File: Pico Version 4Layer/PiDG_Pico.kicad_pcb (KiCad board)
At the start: 4 copper layers, 126 x 126 mm, 70 parts, among them J1 Conn_02x05_Odd_Even, J10 Trig, J11 Laser Enable, J12 Pixel Reset, J14 Pico Socket A, J15 Pico Socket B, J16 Laser En/PWM Trig/GND, J17 USB-C PD in, J2 Conn_02x05_Odd_Even, J3 Conn_02x05_Odd_Even, J4 Conn_02x05_Odd_Even, J5 Conn_02x05_Odd_Even, J6 Conn_02x05_Odd_Even, J7 Laser 1, J8 Laser 2, U1 74LVC1G04, U10 74AHCT1G08, U12 74LVC1G17, U13 UCC27524, U14 CH224K, U15 AP63205WU, U16 LM66100, U17 LP2951D, U2 SN74LVC04AD, U3 74LVC1G04, U4 SN74LVC04AD, U5 74LVC1G04, U6 SN74LVC04AD, U7 74AHCT1G08, U8 74AHCT1G08, U9 NCP718xSN180

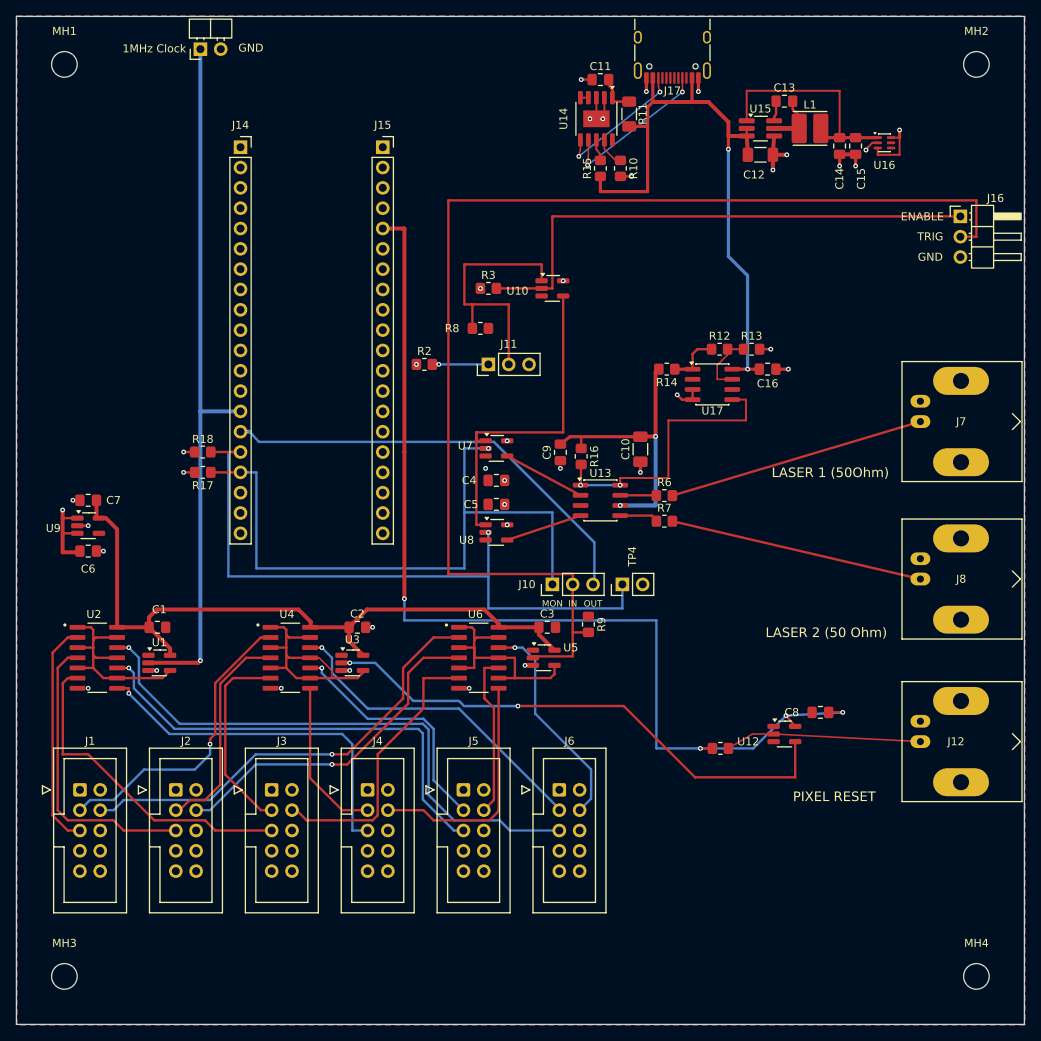
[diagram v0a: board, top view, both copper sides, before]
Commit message: Final DFM/SI review: layout fixes, fresh fab outputs, JLC files, README
Board (Pico Version 4Layer), from a fab / assembly / signal-integrity review:
- U13 decoupling: C9 (0.1 uF 50 V) moved beside VDD pin 6 with its own GND
  via; GND pin 3 gets a direct plane via; +12V via moved under the package;
  R6/R7 shifted 2 mm out to make room. Loop ~1.5-2 nH, was 7-13 nH.
- R19 100 ohm in series with J10 pin 1 (new net CH1_J10): with J10 on 1-2,
  the PWM_TRIG_TAP load made CH1 arrive 0.4-1.7 ns after CH2.
- No vias left inside SMD pads except U14's exposed-pad thermal vias:
  13 moved off their pads (U13 ENA/ENB now joined on F.Cu), 9 nudged clear
  of neighbouring mask openings.
- 47 edge stitching vias and 7 local GND vias at decoupling caps / IC grounds.
- 3 mm copper keep-out around each M3 hole; zone-to-edge clearance 0.5 mm.
- Silkscreen: TP3 reference restored ("1MHz Clock" kept as board text),
  J10 relabelled CH1/TRG/MKR, J11 ON/OFF, Pico outline + USB-end arrow +
  pin-1 mark, references moved off vias.
- U11 (socketed Pico) marked not-on-board / not-in-BOM in the schematic.
DRC 0 violations / 0 unconnected, ERC 0, all 334 pads match the schematic.

Outputs: gerbers, drills and zip regenerated (the previous set predated the
silkscreen edits); BOM/CPL updated (R19, capacitor voltage/dielectric,
loose jumper shunts); fab/jlc/ holds JLC-format SMD BOM and CPL with the
LCSC column left for part selection.

Docs: new top-level README (quick start, connecting, full command reference
with replies captured from the firmware, troubleshooting, wireless as a
future option); tools/pidg_example.py; Hardware.md gains manufacturing notes
and first-power-up checks and loses stale claims (finest pitch, RUN button,
TX_DROPPED unit, J16 interlock, Wi-Fi range).

Co-Authored-By: Claude Opus 5.5 (1M context) <noreply@anthropic.com>
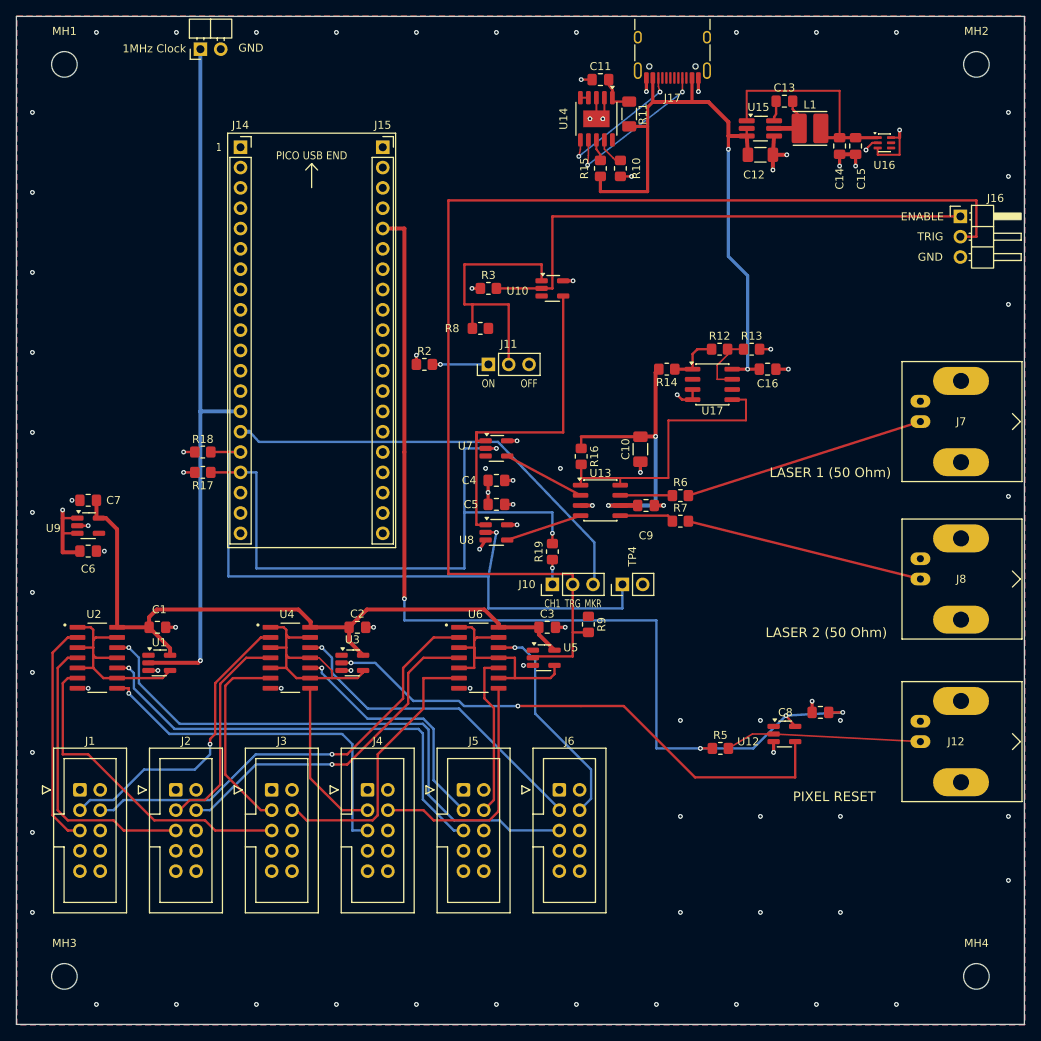
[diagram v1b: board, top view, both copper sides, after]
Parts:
- added R19: 100, Resistor_SMD:R_0805_2012Metric_Pad1.20x1.40mm_HandSolder, F.Cu at (199.0, 96.9)
- TP3: renamed from 1MHz Clock
- moved C9 12.6 mm to (210.7, 91.1), turned to 180 degrees
- moved R6 2.00 mm to (215.0, 89.9)
- moved R7 2.00 mm to (215.0, 93.1)
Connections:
- J10 pad 1: _PULSE_OUT_CH1 -> CH1_J10
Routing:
- net GND: track 39.1 -> 51.7 mm, vias 29 -> 84
- net +5V: track 18.9 -> 26.9 mm
- net _PULSE_OUT_CH1: track 82.1 -> 79.0 mm, vias 1 -> 2
- net CH1_J10: track 0.00 -> 3.10 mm, vias 0 -> 1
- net +12V: track 35.3 -> 37.5 mm
- net CH2_DRIVE_RAW: track 4.86 -> 6.86 mm
- net CH1_DRIVE_RAW: track 4.53 -> 6.53 mm
- net CH2_DRIVE: track 31.8 -> 29.9 mm
- net CH1_DRIVE: track 32.4 -> 30.4 mm
- net _PULSE_OUT_CH2: track 82.9 -> 84.0 mm
- net LASER_PWR_OK: track 35.7 -> 35.6 mm, vias 2 -> 0
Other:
- board text added: "1"
- board text added: "1MHz Clock"
- board text added: "CH1"
- board text added: "LASER 1 (50 Ohm)"
- board text added: "MKR"
- board text added: "OFF"
- board text added: "ON"
- board text added: "PICO USB END"
- board text added: "TRG"
- board text removed: "IN"
- board text removed: "LASER 1 (50Ohm)"
- board text removed: "MON"
- board text removed: "OUT"

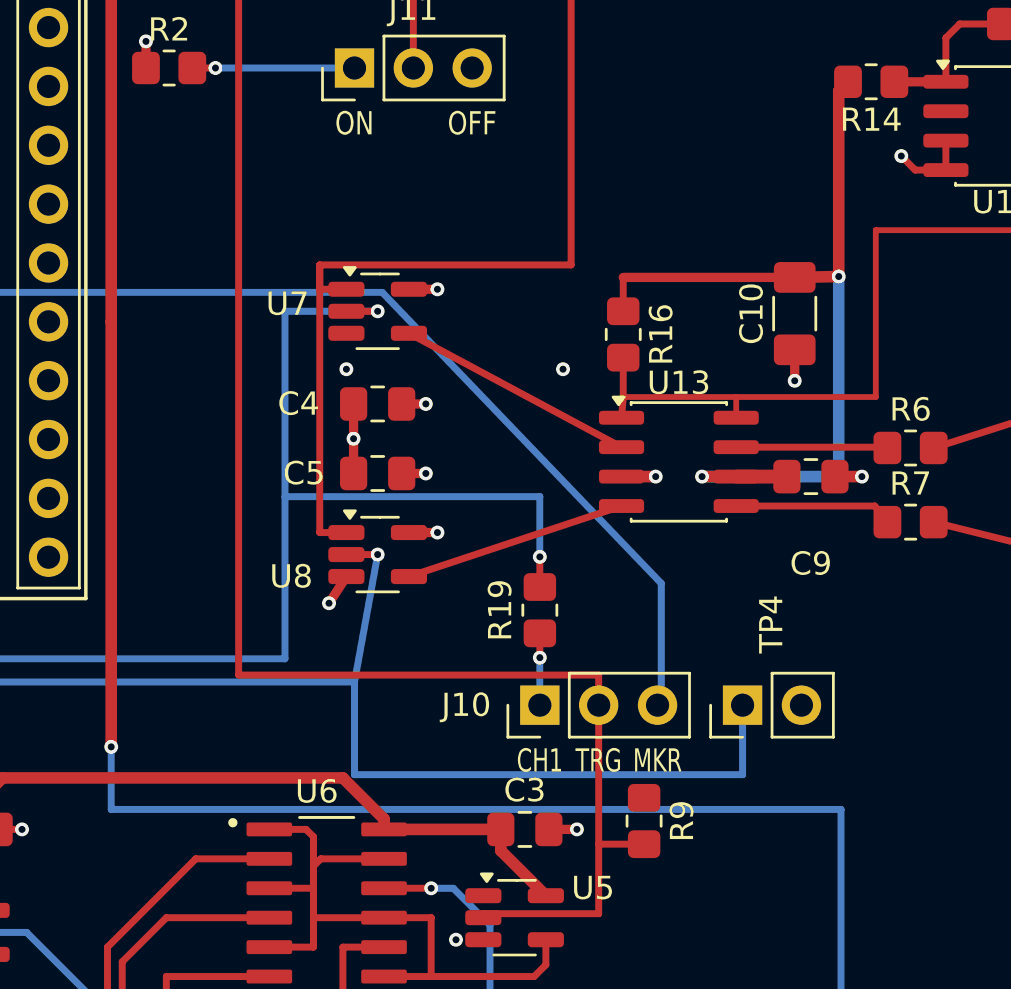
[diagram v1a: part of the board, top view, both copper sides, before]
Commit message: Silkscreen and docs: J11 E-stop wiring, J10 trigger-source key, TP4 CH2 scope point
J11 now reads 'LASER INTERLOCK: ON = 1-2' and 'E-STOP: NC SWITCH ACROSS 1-2';
J10 gets a 'CAMERA TRIGGER: TRG-MKR = MARKER / TRG-CH1 = LASER 1' key (its
reference moved up); TP4 is labelled CH2 / GND / SCOPE ONLY (R9's reference
moved clear). README and Hardware.md explain the fail-safe normally-closed
switch across J11 1-2 and why J16.1 is not an E-stop input. DRC 0/0; gerbers,
drills and zip regenerated.

Co-Authored-By: Claude Opus 5.5 (1M context) <noreply@anthropic.com>
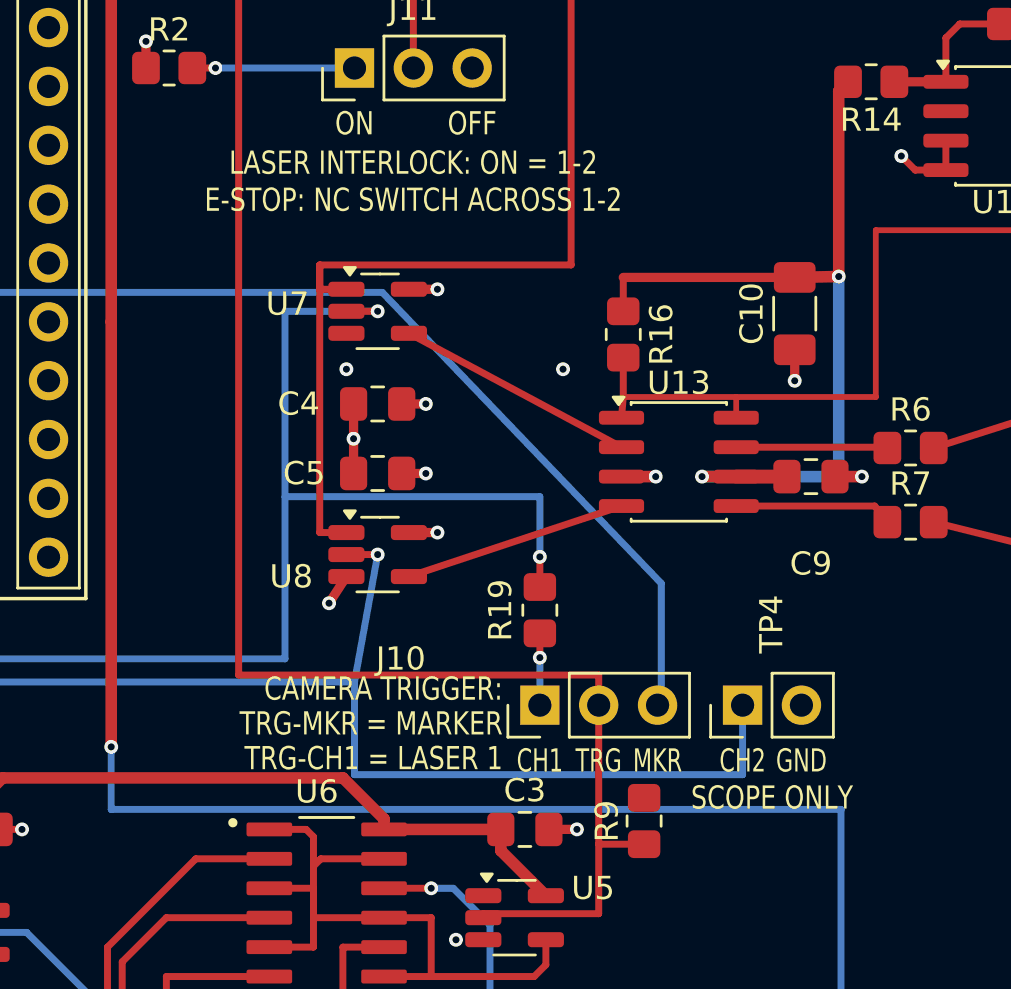
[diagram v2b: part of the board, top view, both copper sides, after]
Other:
- board text added: "CAMERA TRIGGER:"
- board text added: "CH2"
- board text added: "E-STOP: NC SWITCH ACROSS 1-2"
- board text added: "LASER INTERLOCK: ON = 1-2"
- board text added: "SCOPE ONLY"
- board text added: "TRG-CH1 = LASER 1"
- board text added: "TRG-MKR = MARKER"
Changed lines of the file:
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@@
 		(tags "resistor handsolder")
 		(property "Reference" "R9"
-			(at 0 1.65 90)
+			(at 0 -1.6 90)
 			(layer "F.SilkS")
 			(effects
@@
 		(tags "Through hole pin header THT 1x03 2.54mm single row")
 		(property "Reference" "J10"
-			(at 0 -3.175 0)
+			(at 2 -6 0)
 			(layer "F.SilkS")
 			(effects
@@
 		)
 	)
+	(gr_text "CH2"
+		(at 207.75 103.4 0)
+		(layer "F.SilkS")
+		(effects
+			(font
+				(size 1 0.7)
+				(thickness 0.15)
+			)
+		)
+	)
+	(gr_text "GND"
+		(at 210.29 103.4 0)
+		(layer "F.SilkS")
+		(effects
+			(font
+				(size 1 0.7)
+				(thickness 0.15)
+			)
+		)
+	)
 	(gr_text "1"
 		(at 157.3 46.355 0)
@@
 		)
 	)
+	(gr_text "LASER INTERLOCK: ON = 1-2"
+		(at 193.54 77.6 0)
+		(layer "F.SilkS")
+		(effects
+			(font
+				(size 1 0.8)
+				(thickness 0.15)
+			)
+		)
+	)
+	(gr_text "E-STOP: NC SWITCH ACROSS 1-2"
+		(at 193.54 79.2 0)
+		(layer "F.SilkS")
+		(effects
+			(font
+				(size 1 0.8)
+				(thickness 0.15)
+			)
+		)
+	)
 	(gr_text "OFF"
 		(at 196.08 75.9 0)
@@
 		)
 	)
+	(gr_text "SCOPE ONLY"
+		(at 209.02 105 0)
+		(layer "F.SilkS")
+		(effects
+			(font
+				(size 1 0.8)
+				(thickness 0.15)
+			)
+		)
+	)
+	(gr_text "CAMERA TRIGGER:"
+		(at 197.4 100.3 0)
+		(layer "F.SilkS")
+		(effects
+			(font
+				(size 1 0.8)
+				(thickness 0.15)
+			)
+			(justify right)
+		)
+	)
+	(gr_text "TRG-MKR = MARKER"
+		(at 197.4 101.8 0)
+		(layer "F.SilkS")
+		(effects
+			(font
+				(size 1 0.8)
+				(thickness 0.15)
+			)
+			(justify right)
+		)
+	)
+	(gr_text "TRG-CH1 = LASER 1"
+		(at 197.4 103.3 0)
+		(layer "F.SilkS")
+		(effects
+			(font
+				(size 1 0.8)
+				(thickness 0.15)
+			)
+			(justify right)
+		)
+	)

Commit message: JLC full-assembly order package: LCSC numbers for all 67 parts, THT in CPL, checklist
- fab/jlc/PiDG_Pico_JLC_BOM.csv: 34 lines, every one with an LCSC number
  checked against JLC's library (2026-09-25); through-hole connectors and
  headers included so JLC fits everything.
- fab/jlc/PiDG_Pico_JLC_CPL.csv: all 67 parts; through-hole parts at their
  pad centre (footprint origins are on pin 1).
- fab/jlc/JLC_ORDER.md: order-form settings, remarks, parts needing Global
  Sourcing (CH224K and NCP718 out of stock; 69.8R stock thin), rotation
  checks, cost estimate, on-delivery steps and enclosure notes.
- C6/C11 -> 1 uF 50 V (shares C16's basic part), C10 -> 10 uF 50 V (shares
  C12's part): two fewer extended-part fees. Human BOM gains an LCSC column.
- Back silkscreen: JLC order-number placeholder. Gerbers/drills/zip
  regenerated; DRC 0/0, ERC 0.

Co-Authored-By: Claude Opus 5.5 (1M context) <noreply@anthropic.com>
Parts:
- C10: value 10uF 25V -> 10uF 50V
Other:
- board text added: "JLCJLCJLCJLC"
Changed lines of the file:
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@@
 			)
 		)
-		(property "Value" "10uF 25V"
+		(property "Value" "10uF 50V"
 			(at 0 1.85 90)
 			(layer "F.Fab")
@@
 		)
 	)
+	(gr_text "JLCJLCJLCJLC"
+		(at 195 145 0)
+		(layer "B.SilkS")
+		(effects
+			(font
+				(size 1 1)
+				(thickness 0.15)
+			)
+			(justify mirror)
+		)
+	)
